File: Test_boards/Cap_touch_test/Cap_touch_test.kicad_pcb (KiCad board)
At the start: 2 copper layers, 0 parts

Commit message: Complicated pads are beyond my skills at the moment. I will need to create something of 'fill zones'. I reached out some feelers on hackaday but I am proceeding with my current information.
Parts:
- added C1: 0.1uF, Capacitor_SMD:C_0805_2012Metric, F.Cu at (91.8, 34.4)
- added C6: 0.1uF, Capacitor_SMD:C_0805_2012Metric, F.Cu at (86.9, 38.1)
- added C7: 0.1uF, Capacitor_SMD:C_0805_2012Metric, F.Cu at (86.9, 34.8)
- added D1: Red, Diode_SMD:D_0805_2012Metric, F.Cu at (95.9, 23.8)
- added D2: Red, Diode_SMD:D_0805_2012Metric, F.Cu at (99.1, 23.8)
- added D3: Red, Diode_SMD:D_0805_2012Metric, F.Cu at (102.4, 23.8)
- added D4: Red, Diode_SMD:D_0805_2012Metric, F.Cu at (105.7, 23.8)
- added J1: Conn_02x05_Odd_Even, Connector_PinHeader_1.27mm:PinHeader_2x05_P1.27mm_Vertical, F.Cu at (85.3, 18.5)
- added J2: Screw_Terminal_01x02, TerminalBlock:TerminalBlock_bornier-2_P5.08mm, F.Cu at (72.1, 18.8)
- added RN1: R_Pack04, Resistor_SMD:R_Array_Concave_4x0603, F.Cu at (99.4, 17.1)
- added U1: LPC804-TSSOP24, Package_SO:TSSOP-24_4.4x7.8mm_P0.65mm, F.Cu at (87.4, 27.7)
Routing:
- net 3v3: track 0.00 -> 59.7 mm, vias 0 -> 1
- net GND: track 0.00 -> 42.2 mm, vias 0 -> 2
- net LED3: track 0.00 -> 24.6 mm
- net Net-(J1-Pad2): track 0.00 -> 24.2 mm
- net LED2: track 0.00 -> 21.8 mm
- net Net-(J1-Pad4): track 0.00 -> 21.3 mm, vias 0 -> 2
- net ACMP: track 0.00 -> 20.2 mm
- net LED1: track 0.00 -> 19.0 mm
- net LED0: track 0.00 -> 15.7 mm
- net Net-(J1-Pad10): track 0.00 -> 10.8 mm, vias 0 -> 1
- net Net-(D4-Pad2): track 0.00 -> 8.22 mm
- net Net-(D3-Pad2): track 0.00 -> 6.06 mm
- net Net-(D1-Pad2): track 0.00 -> 5.93 mm
- net Net-(D2-Pad2): track 0.00 -> 5.02 mm
- net CAPT_YL: track 0.00 -> 3.21 mm

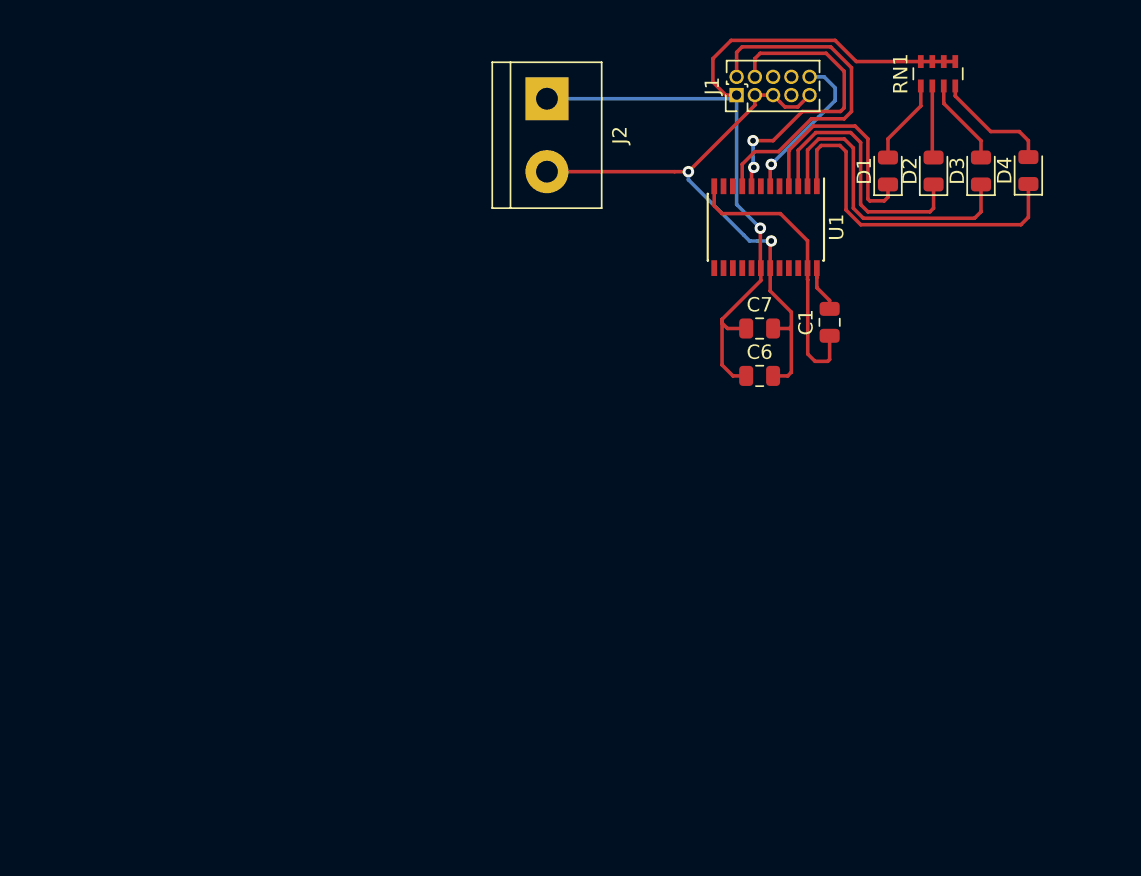
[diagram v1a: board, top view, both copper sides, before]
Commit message: Added test cap touch pads to test board. Added renders. Review before initial submission to PCBway for manufacturing.
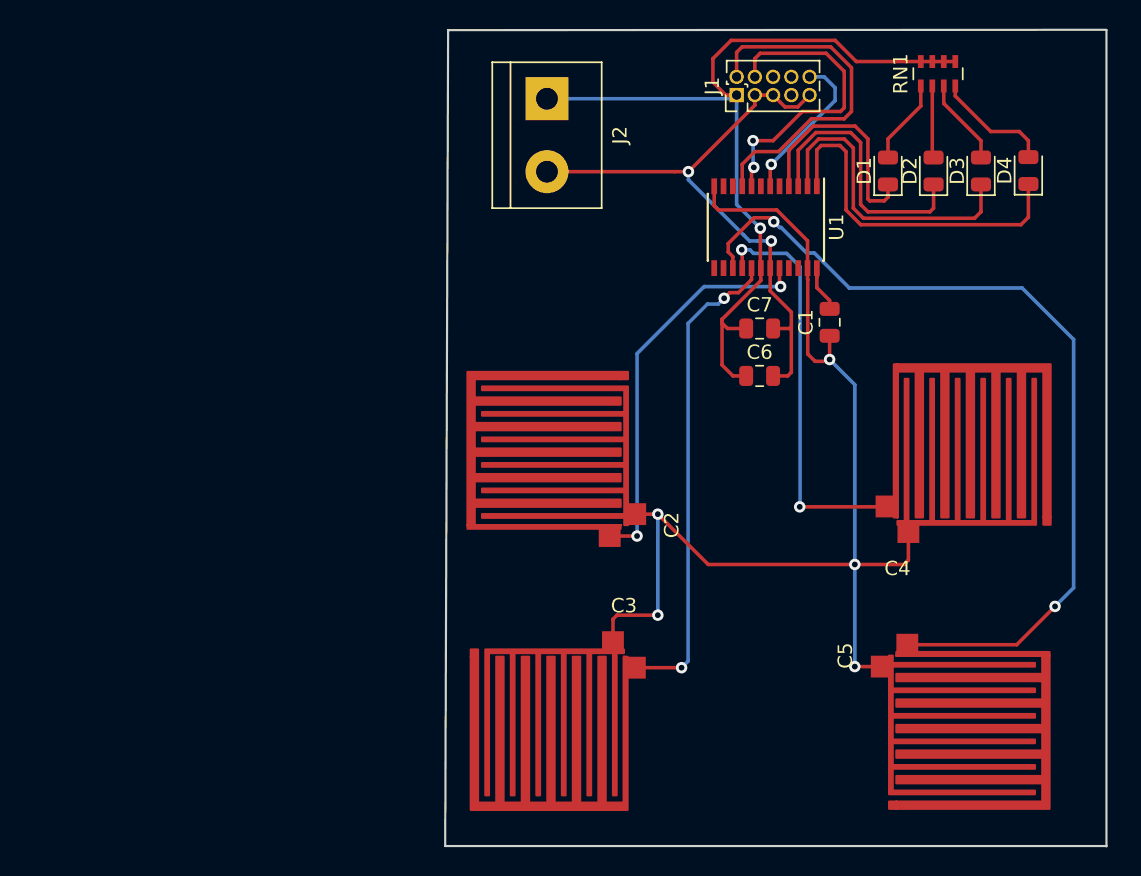
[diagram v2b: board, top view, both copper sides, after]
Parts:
- added C2: CAPT, cap_touch_LPC804_NXP:Cap_T_pad, F.Cu at (77.3, 48.5)
- added C3: CAPT, cap_touch_LPC804_NXP:Cap_T_pad, F.Cu at (77.5, 57.7)
- added C4: CAPT, cap_touch_LPC804_NXP:Cap_T_pad, F.Cu at (96.5, 48.0)
- added C5: CAPT, cap_touch_LPC804_NXP:Cap_T_pad, F.Cu at (96.5, 57.6)
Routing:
- net CAPT_X3: track 0.00 -> 60.7 mm, vias 0 -> 2
- net ACMP: track 20.2 -> 78.6 mm, vias 0 -> 5
- net CAPT_X1: track 0.00 -> 33.9 mm, vias 0 -> 2
- net CAPT_X2: track 0.00 -> 28.6 mm, vias 0 -> 2
- net CAPT_X0: track 0.00 -> 28.1 mm, vias 0 -> 2
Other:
- board outline added: 46.1 x 56.9 mm

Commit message: Test boards submitted to PCBway for review and approval.
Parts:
- C2, C3, C4, C5: footprint cap_touch_LPC804_NXP:Cap_T_pad -> cap_touch_LPC804_NXP:Cap_T_pad_v1.1
- moved C4 41.1 mm to (56.1, 40.7), turned to 90 degrees
- moved C5 36.3 mm to (64.9, 39.8), turned to 0 degrees
- moved C3 23.1 mm to (56.4, 48.1)
- moved C2 11.8 mm to (65.5, 47.8), turned to 270 degrees
- moved J2 0.54 mm to (72.6, 19.0), turned to 180 degrees
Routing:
- net CAPT_X1: track 33.9 -> 103.7 mm, vias 2 -> 0
- net CAPT_X2: track 28.6 -> 67.3 mm, vias 2 -> 0
- net CAPT_X3: track 60.7 -> 33.9 mm, vias 2 -> 0
- net CAPT_X0: track 28.1 -> 36.8 mm, vias 2 -> 0
- net GND: track 42.2 -> 48.8 mm, vias 2 -> 1
- net ACMP: track 78.6 -> 83.0 mm, vias 5 -> 2
- added copper zone on B.Cu, net GND
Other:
- board size 46.1 x 56.9 mm -> 75 x 47.8 mm
- board text added: "Cap Touch Test Board"
